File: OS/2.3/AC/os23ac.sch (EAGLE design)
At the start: 121 parts, among them T1 Z0103MN0, T2 Z0103MN, T3 Z0103MN, T4 Z0103MN, T5 Z0103MN, T6 Z0103MN, T7 Z0103MN, T8 Z0103MN, X0 32.768kHz

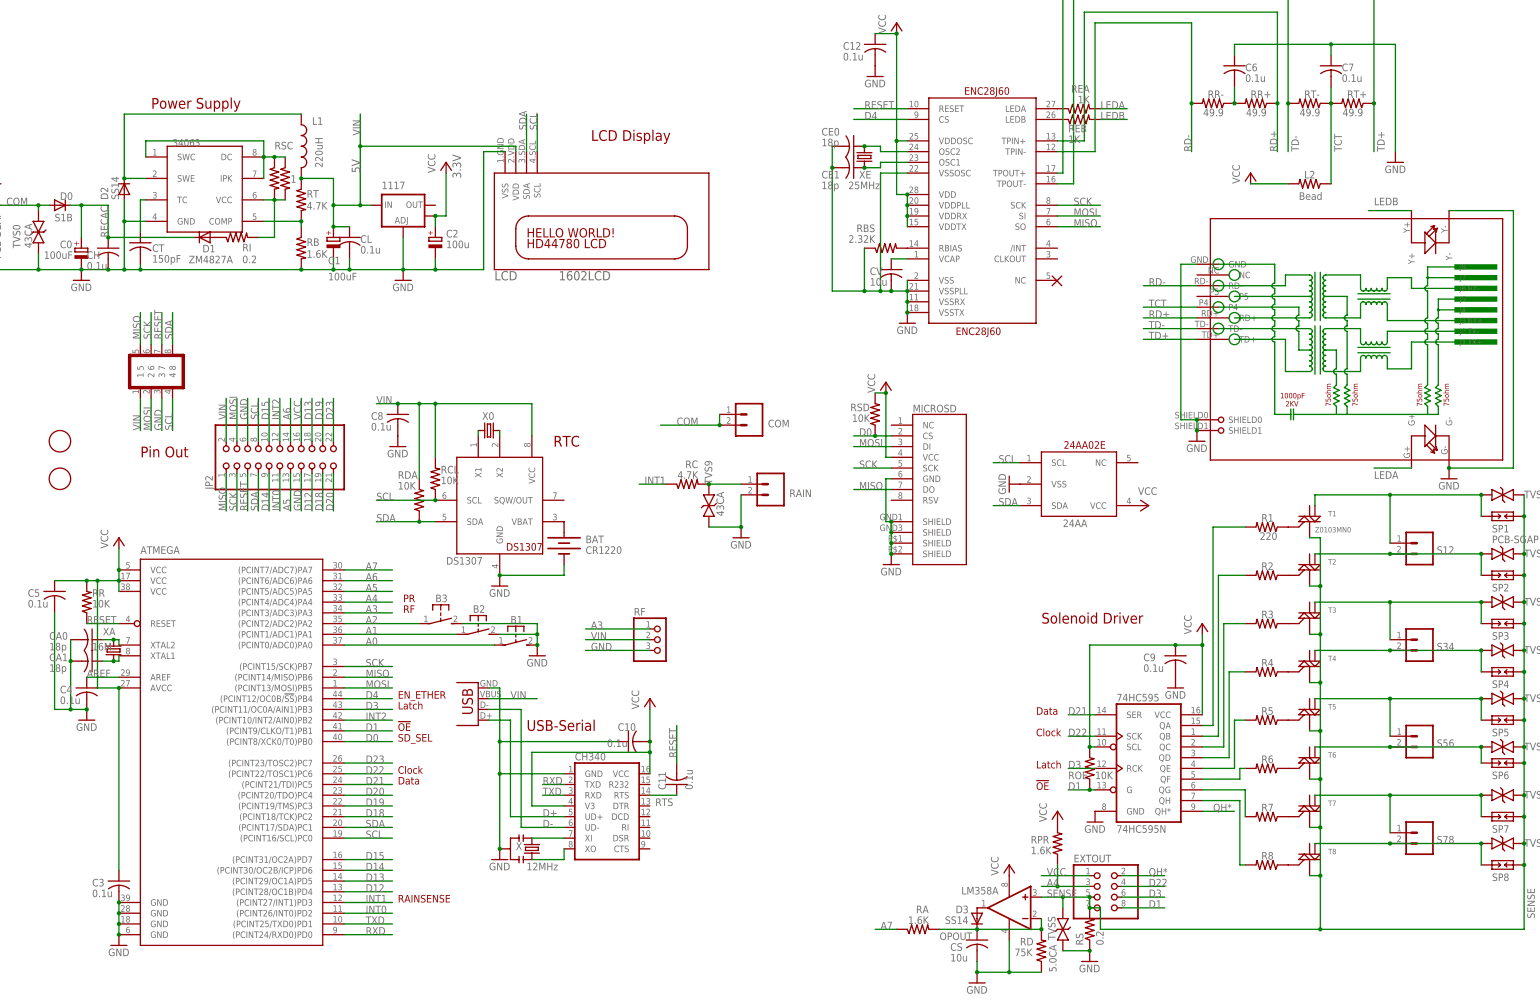
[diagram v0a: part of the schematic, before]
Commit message: add image exports for os2.3 hardware design files
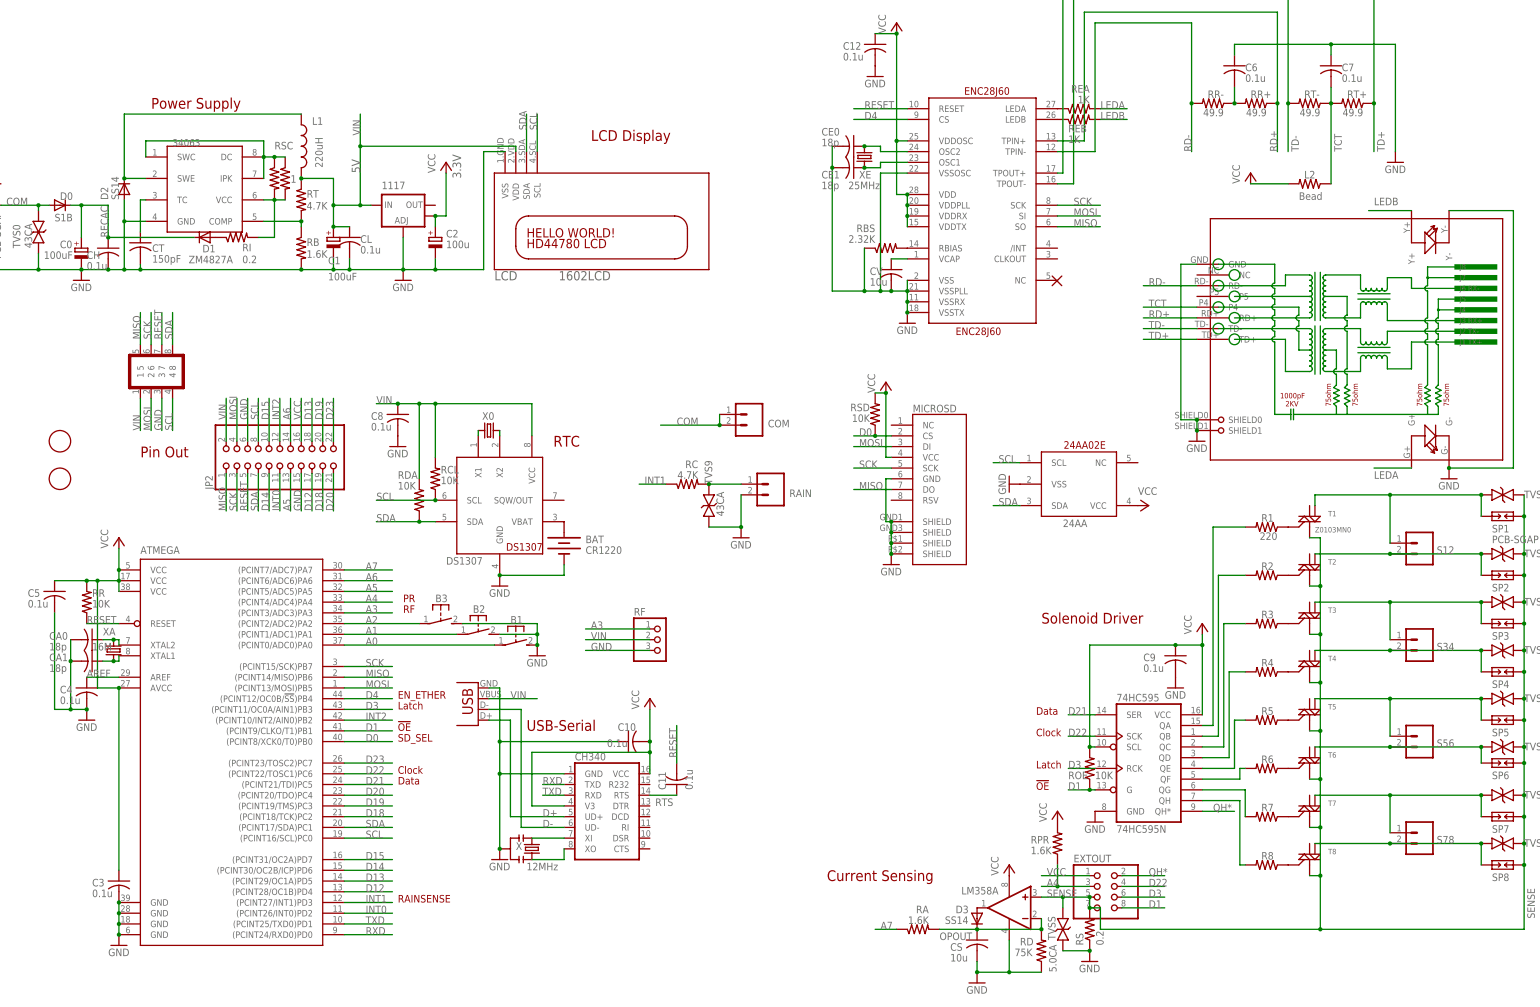
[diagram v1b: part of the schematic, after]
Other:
- note added: "Current Sensing"
